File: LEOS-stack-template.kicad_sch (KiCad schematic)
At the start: 19 parts, among them J1 MicroFit_1x4, J2 MicroFit_1x4, U1 MCP2562FD, U2 MCP2518FD, Y1 40 MHz

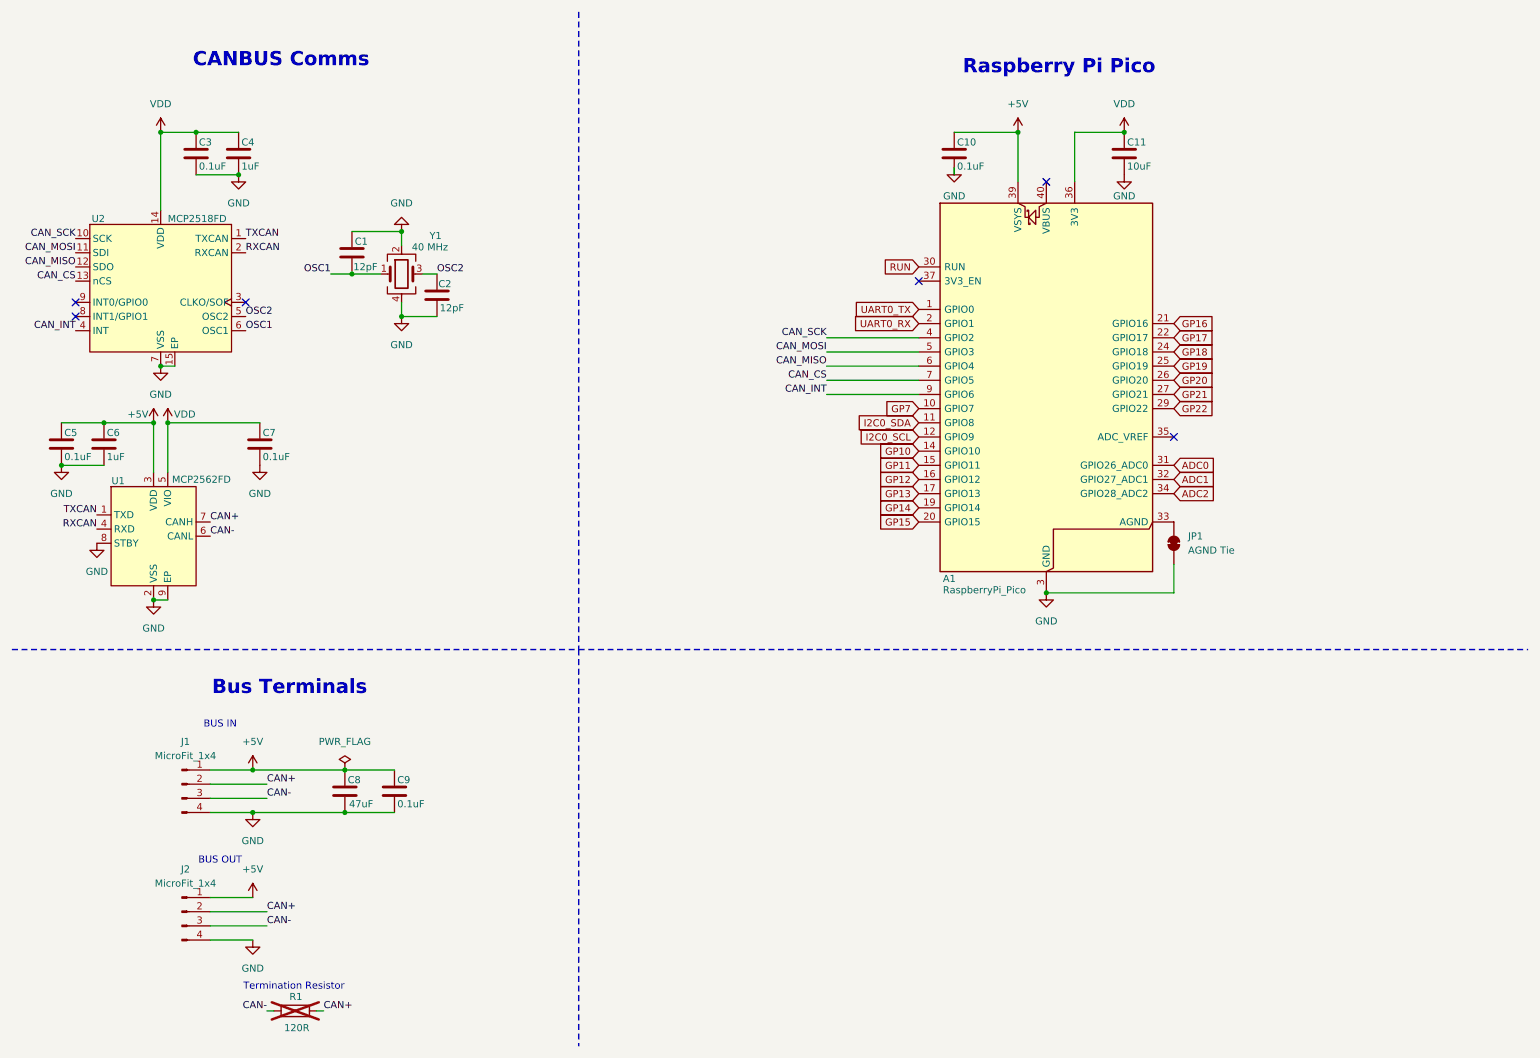
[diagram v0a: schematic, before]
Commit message: Added buck converter and components, plus their values
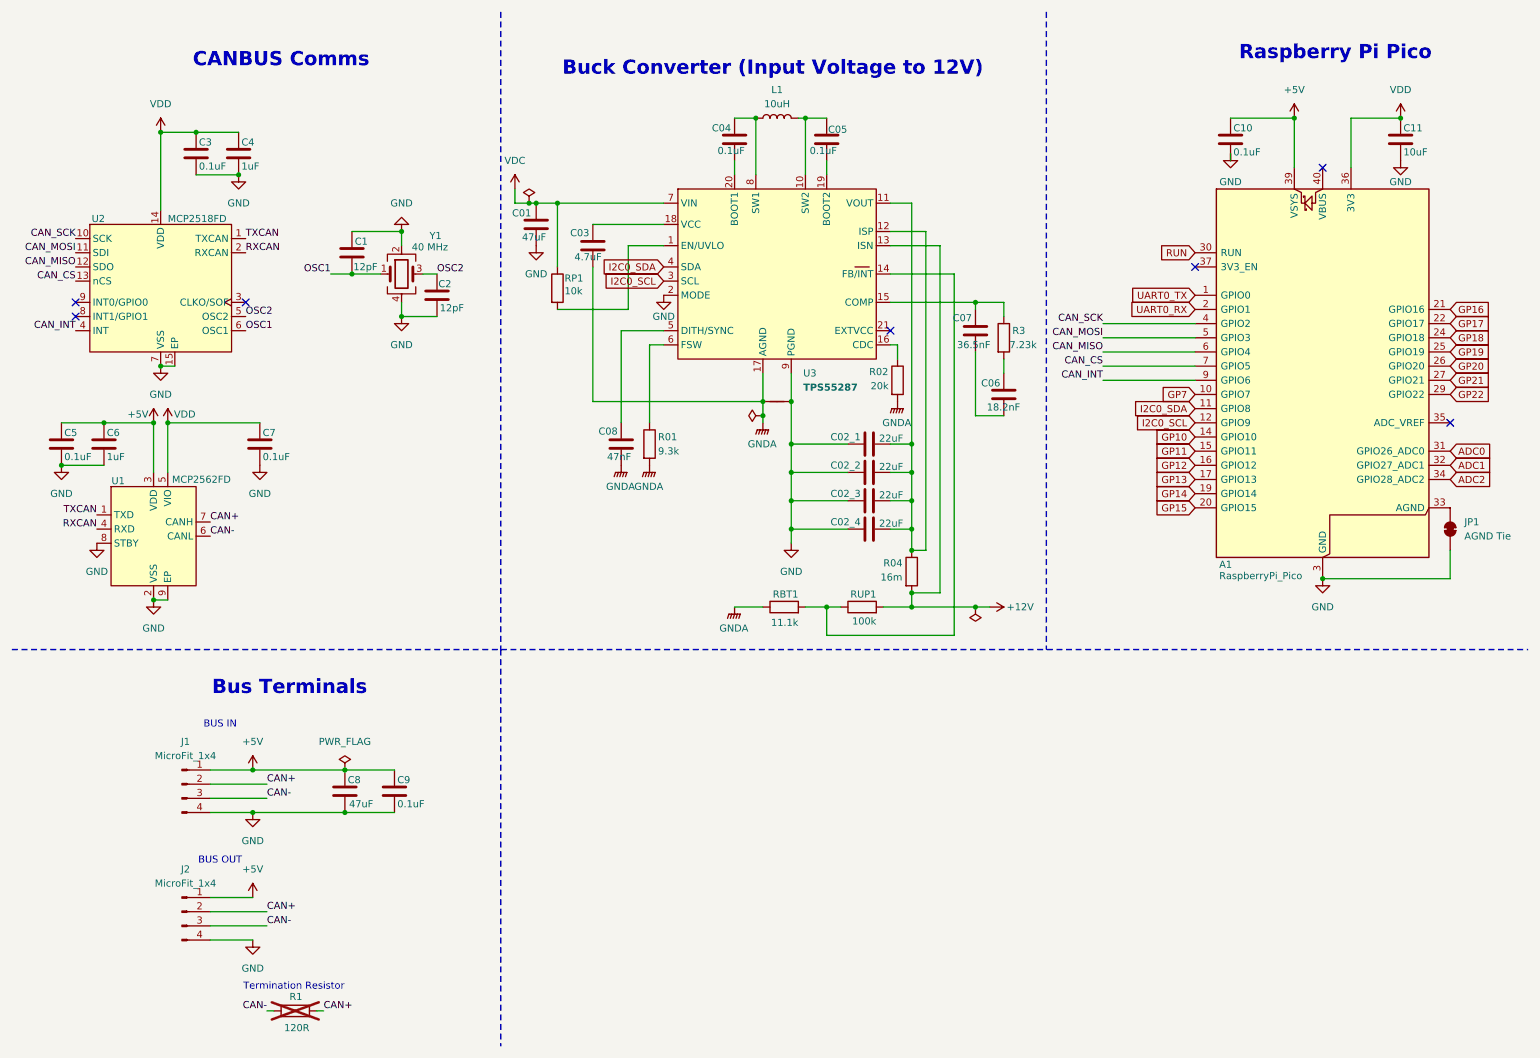
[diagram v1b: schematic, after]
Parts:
- added C01: 47uF, symbol Device:C
- added C02_1, C02_2, C02_3, C02_4: 22uF, symbol Device:C
- added C03: 4.7uF, symbol Device:C
- added C04, C05: 0.1uF, symbol Device:C
- added C06: 18.2nF, symbol Device:C
- added C07: 36.5nF, symbol Device:C
- added C08: 47nF, symbol Device:C
- added L1: 10uH, symbol Device:L
- added NT1: NetTie_2, symbol Device:NetTie_2
- added R01: 9.3k, symbol Device:R
- added R02: 20k, symbol Device:R
- added R04: 16m, symbol Device:R
- added R3: 7.23k, symbol Device:R
- added RBT1: 11.1k, symbol Device:R
- added RP1: 10k, symbol Device:R
- added RUP1: 100k, symbol Device:R
- added U3: TPS55287, LEOS:VQFN21_RYQ_TEX, symbol LEOS:TPS55287
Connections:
- net GND: now also C01.2, C02_1.1, C02_2.1, C02_3.1, C02_4.1, NT1.2, U3.2 (MODE), U3.9 (PGND)
- net I2C0_SCL: now also U3.3 (SCL)
- net I2C0_SDA: now also U3.4 (SDA)
- new net: C02_1.2, C02_2.2, C02_3.2, C02_4.2, R04.1, U3.11 (VOUT), U3.12 (ISP)
- new net: C04.1, L1.1, U3.8 (SW1)
- new net: C04.2, U3.20 (BOOT1)
- new net: C05.1, L1.2, U3.10 (SW2)
- new net: C05.2, U3.19 (BOOT2)
- new net: RBT1.2, RUP1.1, U3.14 (FB/INT)
- new net: R01.1, U3.6 (FSW)
- new net: C03.1, U3.18 (VCC)
- new net: C07.1, R3.1, U3.15 (COMP)
- new net: C06.2, C07.2
- new net: C06.1, R3.2
- new net: RP1.2, U3.1 (EN/UVLO)
- new net: C08.1, U3.5 (DITH/SYNC)
- new net: R02.1, U3.16 (CDC)
- new net +12V: R04.2, RUP1.2, U3.13 (ISN)
- new net GNDA: C03.2, C08.2, NT1.1, R01.2, R02.2, RBT1.1, U3.17 (AGND)
- new net VDC: C01.1, RP1.1, U3.7 (VIN)
- no-connect marks 6 -> 7
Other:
- note added: "Buck Converter (Input Voltage to 12V)"
- moved on the sheet: A1, C10, C11, JP1

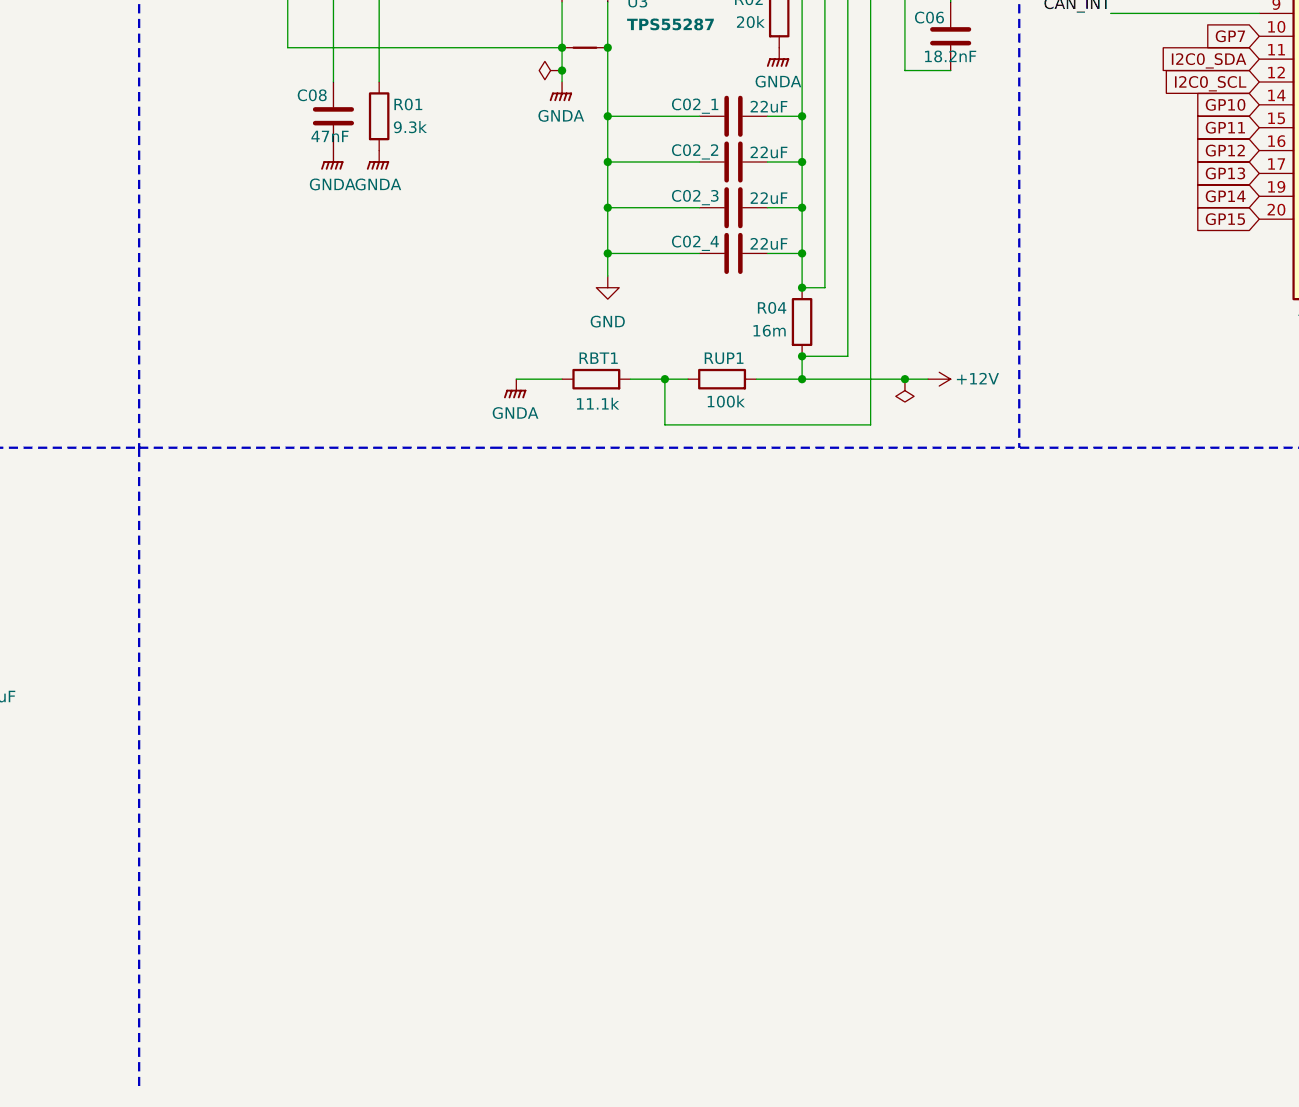
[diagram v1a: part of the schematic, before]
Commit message: Added the 12-5V buck converter to the schematic
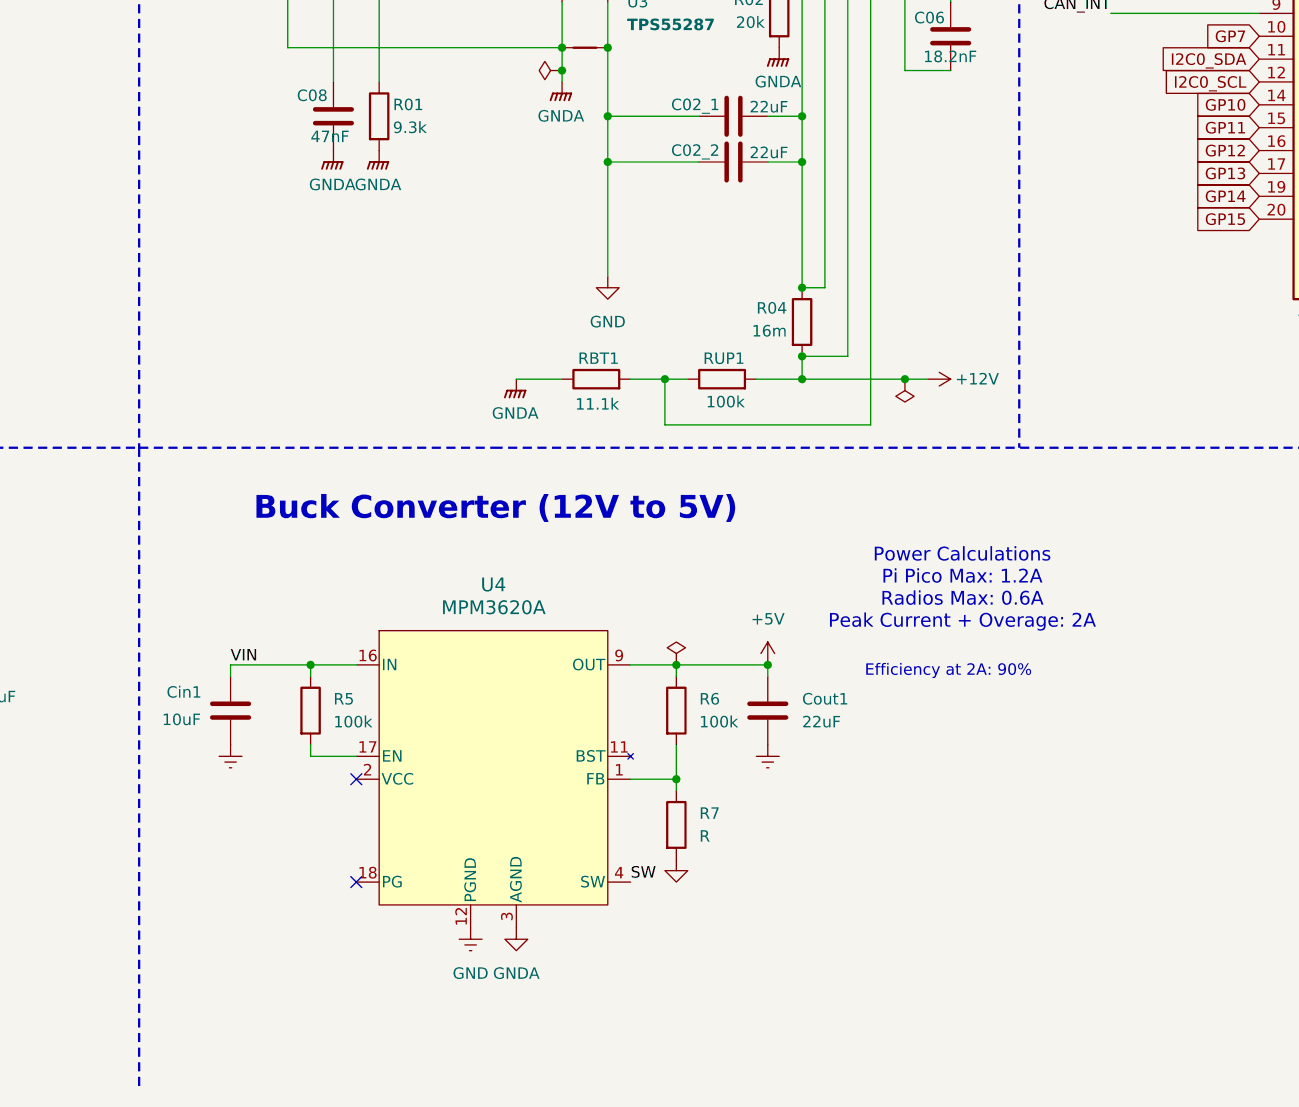
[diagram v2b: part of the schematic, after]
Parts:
- removed C02_3, C02_4: 22uF, symbol Device:C
- added Cin1: 10uF, symbol Device:C
- added Cout1: 22uF, symbol Device:C
- added R5, R6: 100k, symbol Device:R
- added R7: R, symbol Device:R
- added U4: MPM3620A, CustomFootprints:IC18_MPM3620AGQV-Z_MNP, symbol LEOS:MPM3620AGQV-Z
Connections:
- net +5V: now also Cout1.1, R6.1, U4.22 (OUT), U4.7 (OUT), U4.8 (OUT), U4.9 (OUT)
- net GND: now also R7.2, U4.12 (PGND), U4.13 (PGND), U4.14 (PGND)
- net GNDA: now also U4.3 (AGND)
- new net: R6.2, R7.1, U4.1 (FB)
- new net: R5.2, U4.17 (EN)
- new net GNDREF: Cin1.2, Cout1.2
- new net SW: U4.21 (SW), U4.4 (SW), U4.5 (SW), U4.6 (SW)
- new net VIN: Cin1.1, R5.1, U4.16 (IN)
- no-connect marks 7 -> 9
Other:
- note added: "Buck Converter (12V to 5V)"
- note added: "Efficiency at 2A: 90%"
- note added: "Power Calculations Pi Pico Max: 1.2A Radios Max: 0.6A Peak Current + Overage: 2A"

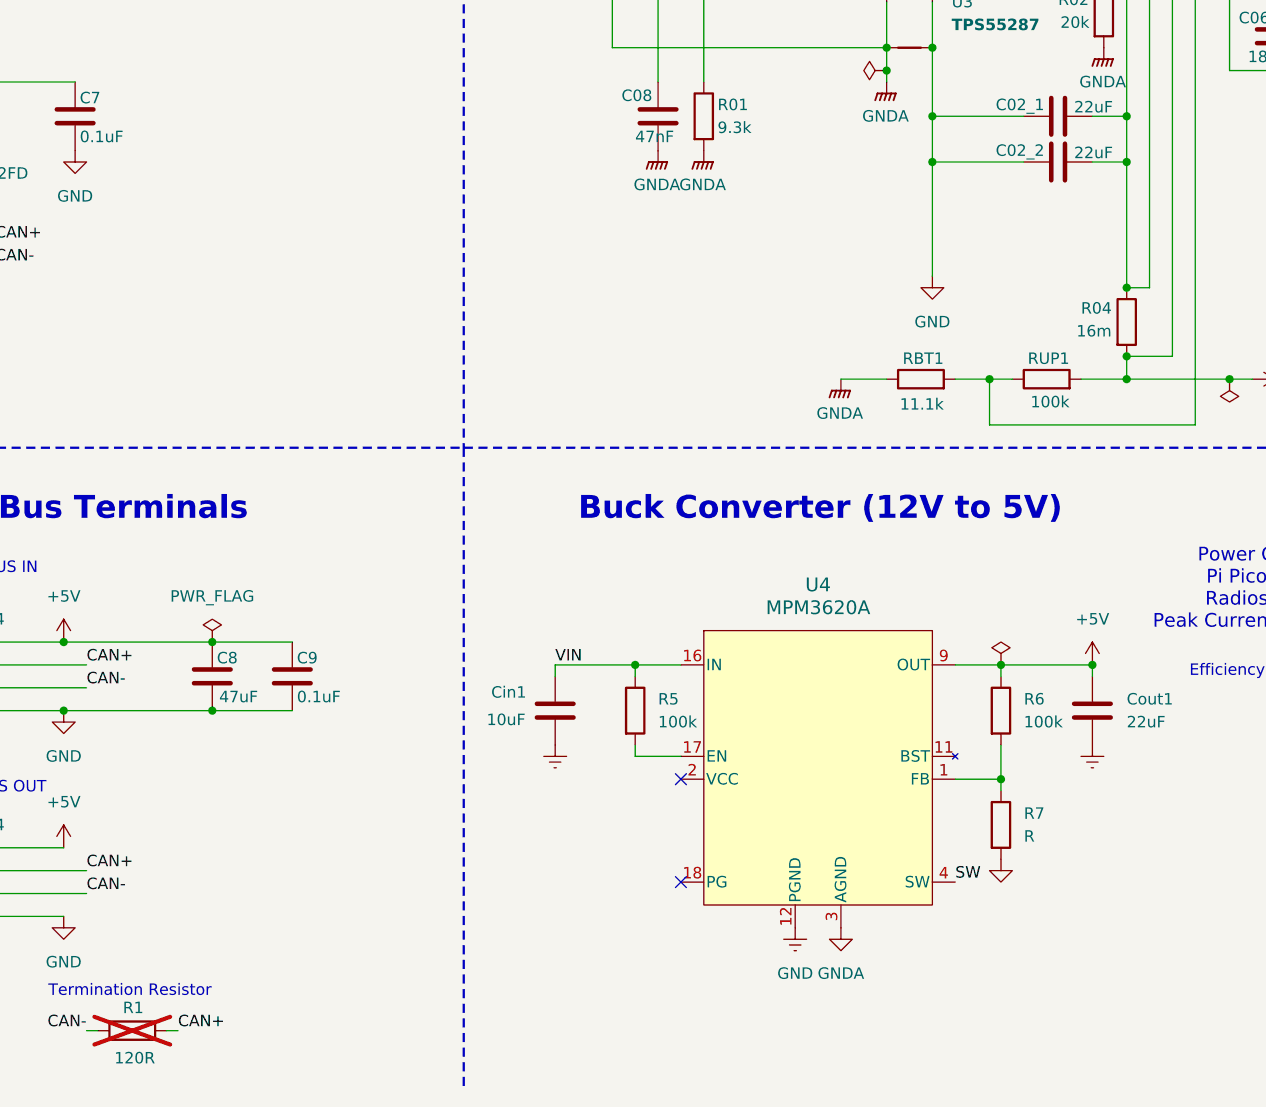
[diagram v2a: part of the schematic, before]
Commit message: updates to schematic and added footprints
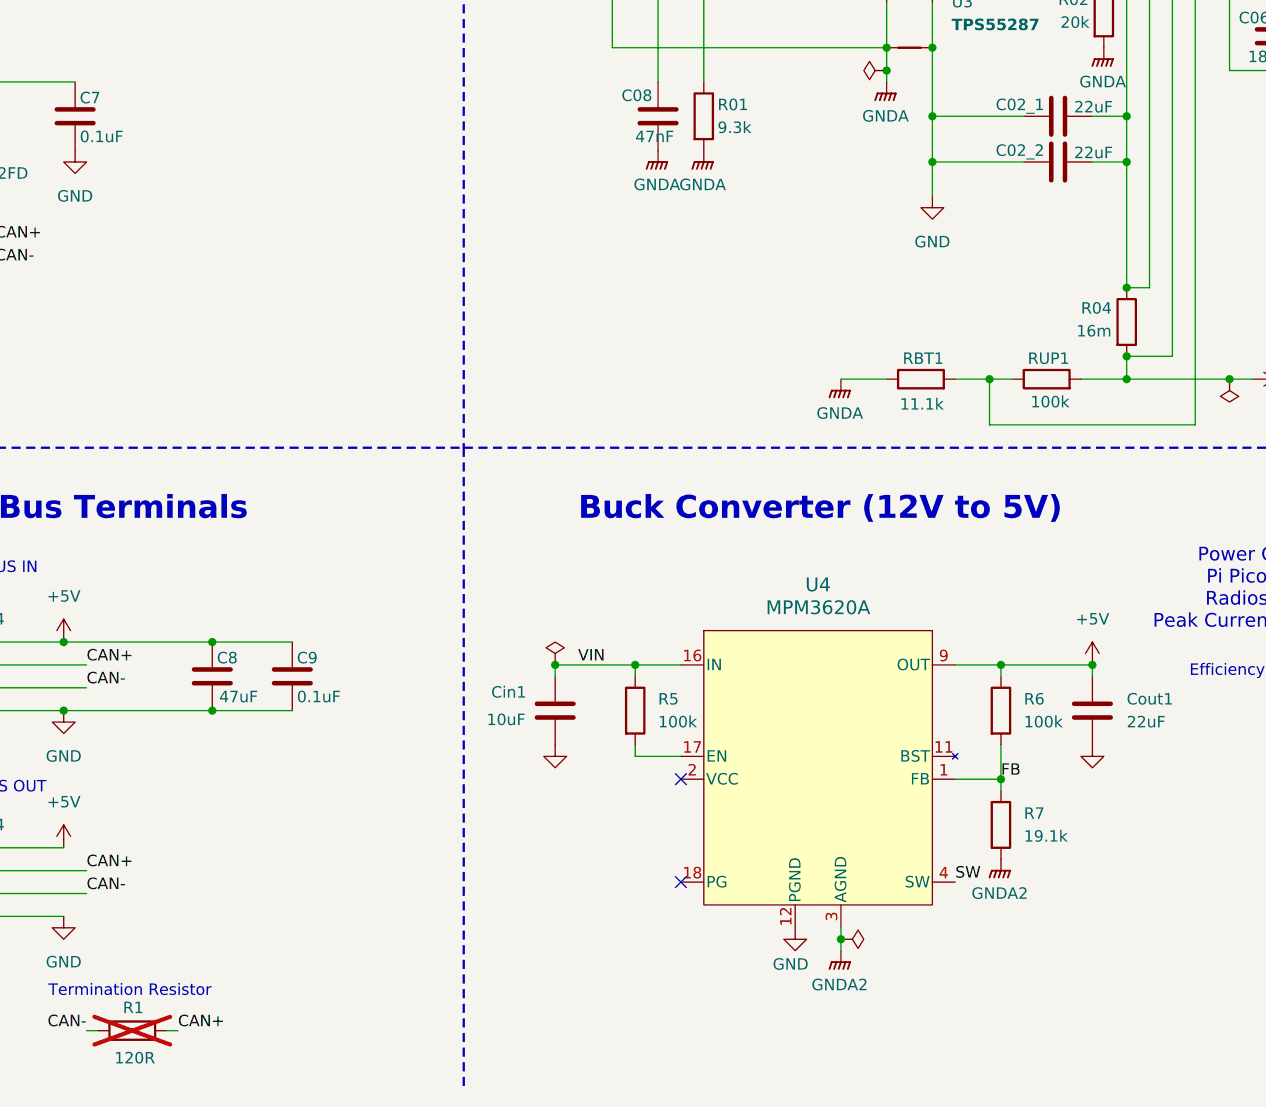
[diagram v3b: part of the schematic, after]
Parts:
- C02_1, C02_2, C03, C04, C05, C07, Cin1, Cout1: footprint (none) -> Capacitor_SMD:C_1206_3216Metric
- L1: footprint (none) -> LEOS:IND_TAIYO_NRS8030_TAY
- R01, R02, R04, R3, R5, R6, RBT1, RP1, RUP1: footprint (none) -> Resistor_SMD:R_0805_2012Metric_Pad1.20x1.40mm_HandSolder
- R7: value R -> 19.1k; footprint (none) -> Resistor_SMD:R_0805_2012Metric_Pad1.20x1.40mm_HandSolder
- U4: footprint CustomFootprints:IC18_MPM3620AGQV-Z_MNP -> LEOS:IC18_MPM3620AGQV-Z_MNP
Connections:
- net GNDREF is gone; now on net GND: Cin1.2, Cout1.2
- net GND: no longer R7.2
- net GNDA: no longer U4.3 (AGND)
- net FB: now reaches R6.2, R7.1, U4.1 (FB)
- new net GNDA2: R7.2, U4.3 (AGND)
